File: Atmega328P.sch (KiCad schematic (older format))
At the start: 20 parts, among them J1 AVR-ISP-6, J2 FTDI, SW1 Reset, U1 LM1117-5.0, U2 ATmega328P-AU, Y1 Crystal

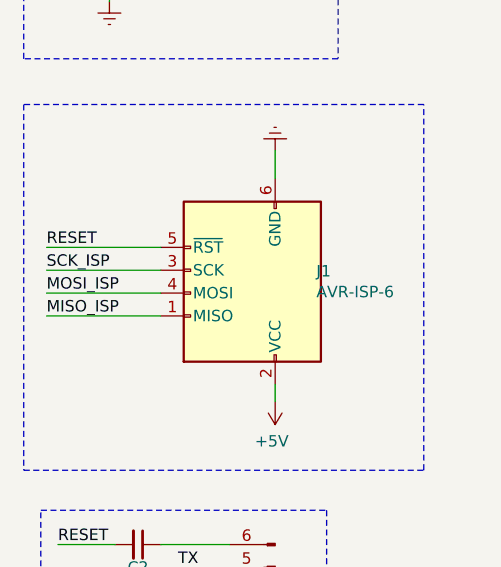
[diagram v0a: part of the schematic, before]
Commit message: Adds an alternative board layout and new footprints.
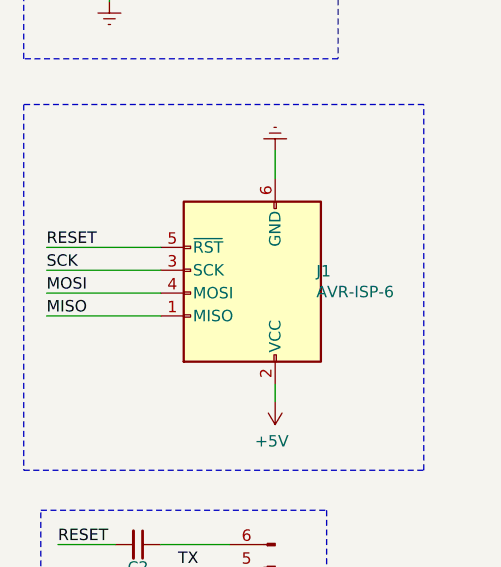
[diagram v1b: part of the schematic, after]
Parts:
- J1: footprint custom:AVR-ISP-6 -> custom:IDC-Header_2x03_Pitch2.54mm_Straight
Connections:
- net D11: no longer J1.4 (MOSI)
- net D12: no longer J1.1 (MISO)
- net D13: no longer J1.3 (SCK)
- net MISO: now also J1.1 (MISO)
- net MOSI: now also J1.4 (MOSI)
- net SCK: now also J1.3 (SCK)
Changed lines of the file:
@@
 F 0 "J1" H 1445 3954 50  0000 R CNN
 F 1 "AVR-ISP-6" H 1445 4045 50  0000 R CNN
-F 2 "custom:AVR-ISP-6" V 1475 4000 50  0001 C CNN
+F 2 "custom:IDC-Header_2x03_Pitch2.54mm_Straight" V 1475 4000 50  0001 C CNN
 F 3 " ~" H 450 3400 50  0001 C CNN
 	1    1725 3950
@@
 Wire Notes Line
 	700  1750 2100 1750
-Wire Notes Line
-	2100 1750 2100 575
 Wire Notes Line
 	2100 575  700  575
@@
 	4775 1700 5850 1700
 Text Label 825  4050 0    50   ~ 0
-MOSI_ISP
+MOSI
 Text Label 825  4150 0    50   ~ 0
-MISO_ISP
+MISO
 Text Label 825  3950 0    50   ~ 0
-SCK_ISP
+SCK
 Text Label 825  3850 0    50   ~ 0
 RESET
@@
 Text Label 1750 2675 0    50   ~ 0
 RESET
+Wire Notes Line
+	2100 1750 2100 575
 $EndSCHEMATC
